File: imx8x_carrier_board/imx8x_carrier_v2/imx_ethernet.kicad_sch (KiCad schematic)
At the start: 91 parts, among them Q1 IRLML6401, Q2 BSS138, U1 DP83867IRRGZR, U10 MCP1824T-ADJE/OT, U2 74AUP1G08, U3 74LVC2G07, U9 TLV71310PDQNR, Y1 25MHz

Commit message: Minor Improvements
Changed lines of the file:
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@@
 		)
 		(property "Value" "GNDPWR"
-			(at 169.926 173.99 0)
+			(at 168.91 173.99 0)
 			(effects
 				(font

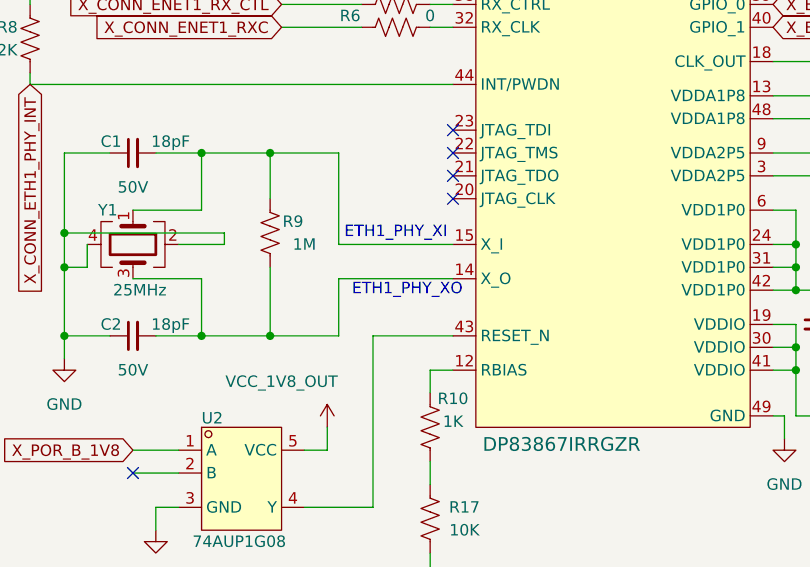
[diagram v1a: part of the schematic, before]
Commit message: Addded Missing Resistor
Dev Kit has Resistor R456, which we did not have included, we have now added it as R93
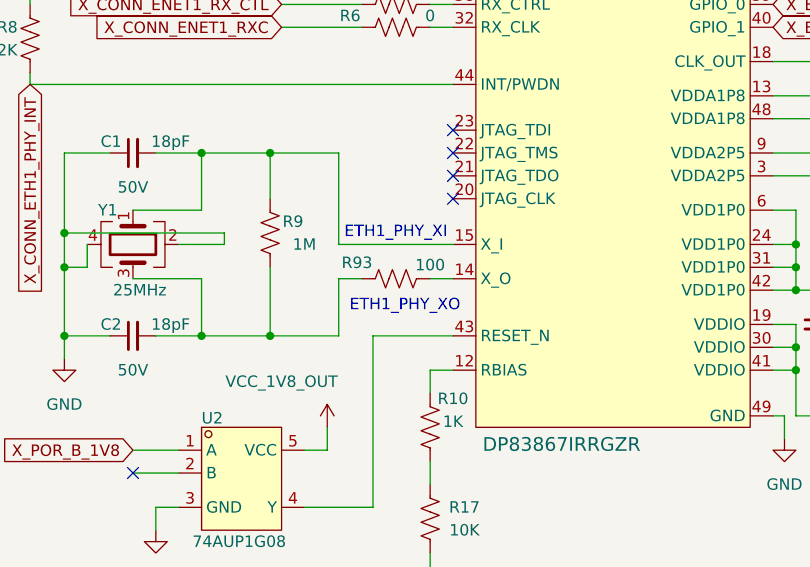
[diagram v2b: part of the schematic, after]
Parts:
- added R93: 100, Resistor_SMD:R_0402_1005Metric, symbol Device:R_US
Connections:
- net at C2.2, R9.2, Y1.3: now also R93.1; no longer U1.14 (X_O)
- new net: R93.2, U1.14 (X_O)
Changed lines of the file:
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@@
 	(text "ETH1_PHY_XO\n"
 		(exclude_from_sim no)
-		(at 69.85 102.87 0)
+		(at 69.596 104.648 0)
 		(effects
 			(font
@@
 	(wire
 		(pts
+			(xy 64.77 101.6) (xy 62.23 101.6)
+		)
+		(stroke
+			(width 0)
+			(type default)
+		)
+	)
+	(wire
+		(pts
 			(xy 220.98 200.66) (xy 261.62 200.66)
 		)
@@
 	(wire
 		(pts
-			(xy 74.93 101.6) (xy 62.23 101.6)
+			(xy 74.93 101.6) (xy 72.39 101.6)
 		)
 		(stroke
@@
 					(unit 1)
 				)
+			)
+		)
+	)
+	(symbol
+		(lib_id "Device:R_US")
+		(at 68.58 101.6 90)
+		(unit 1)
+		(exclude_from_sim no)
+		(in_bom yes)
+		(on_board yes)
+		(dnp no)
+		(property "Reference" "R93"
+			(at 64.262 99.822 90)
+			(effects
+				(font
+					(size 1.27 1.27)
+				)
+			)
+		)
+		(property "Value" "100"
+			(at 72.39 100.076 90)
+			(effects
+				(font
+					(size 1.27 1.27)
+				)
+			)
+		)
+		(property "Footprint" "Resistor_SMD:R_0402_1005Metric"
+			(at 68.834 100.584 90)
+			(effects
+				(font
+					(size 1.27 1.27)
+				)
+				(hide yes)
+			)
+		)
+		(property "Datasheet" "~"
+			(at 68.58 101.6 0)
+			(effects
+				(font
+					(size 1.27 1.27)
+				)
+				(hide yes)
+			)
+		)
+		(property "Description" "Resistor, US symbol"
+			(at 68.58 101.6 0)
+			(effects
+				(font
+					(size 1.27 1.27)
+				)
+				(hide yes)
+			)
+		)
+		(property "LCSC" ""
+			(at 68.58 101.6 0)
+			(effects
+				(font
+					(size 1.27 1.27)
+				)
+			)
+		)
+		(property "Voltage" ""
+			(at 68.58 101.6 0)
+			(effects
+				(font
+					(size 1.27 1.27)
+				)
+			)
+		)
+		(pin "1"
+		)
+		(pin "2"
+		)
+		(instances
+			(project "imx8x_carrier_v2"
+				(path "/4409cb5c-c5cc-45e5-ba22-666413441047/79e8fd09-705e-4c65-82d4-d8130e394a75"
+					(reference "R93")
+					(unit 1)
+				)

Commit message: Renamed something and reverted v2 to original production version
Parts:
- removed R93: 100, Resistor_SMD:R_0402_1005Metric, symbol Device:R_US
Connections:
- net at U1.14 (X_O): now also C2.2, R9.2, Y1.3
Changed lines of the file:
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@@
 	(wire
 		(pts
-			(xy 64.77 101.6) (xy 62.23 101.6)
+			(xy 62.23 101.6) (xy 74.93 101.6)
 		)
 		(stroke
@@
 	(wire
 		(pts
-			(xy 74.93 101.6) (xy 72.39 101.6)
-		)
-		(stroke
-			(width 0)
-			(type default)
-		)
-	)
-	(wire
-		(pts
 			(xy 44.45 127) (xy 41.91 127)
 		)
@@
 					(unit 1)
 				)
-			)
-		)
-	)
-	(symbol
-		(lib_id "Device:R_US")
-		(at 68.58 101.6 90)
-		(unit 1)
-		(exclude_from_sim no)
-		(in_bom yes)
-		(on_board yes)
-		(dnp no)
-		(property "Reference" "R93"
-			(at 64.262 99.822 90)
-			(effects
-				(font
-					(size 1.27 1.27)
-				)
-			)
-		)
-		(property "Value" "100"
-			(at 72.39 100.076 90)
-			(effects
-				(font
-					(size 1.27 1.27)
-				)
-			)
-		)
-		(property "Footprint" "Resistor_SMD:R_0402_1005Metric"
-			(at 68.834 100.584 90)
-			(effects
-				(font
-					(size 1.27 1.27)
-				)
-				(hide yes)
-			)
-		)
-		(property "Datasheet" "~"
-			(at 68.58 101.6 0)
-			(effects
-				(font
-					(size 1.27 1.27)
-				)
-				(hide yes)
-			)
-		)
-		(property "Description" "Resistor, US symbol"
-			(at 68.58 101.6 0)
-			(effects
-				(font
-					(size 1.27 1.27)
-				)
-				(hide yes)
-			)
-		)
-		(property "LCSC" ""
-			(at 68.58 101.6 0)
-			(effects
-				(font
-					(size 1.27 1.27)
-				)
-			)
-		)
-		(property "Voltage" ""
-			(at 68.58 101.6 0)
-			(effects
-				(font
-					(size 1.27 1.27)
-				)
-			)
-		)
-		(pin "1"
-		)
-		(pin "2"
-		)
-		(instances
-			(project "imx8x_carrier_v2"
-				(path "/4409cb5c-c5cc-45e5-ba22-666413441047/79e8fd09-705e-4c65-82d4-d8130e394a75"
-					(reference "R93")
-					(unit 1)
-				)
